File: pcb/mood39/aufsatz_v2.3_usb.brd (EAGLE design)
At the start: 21 x 29 mm, 9 parts

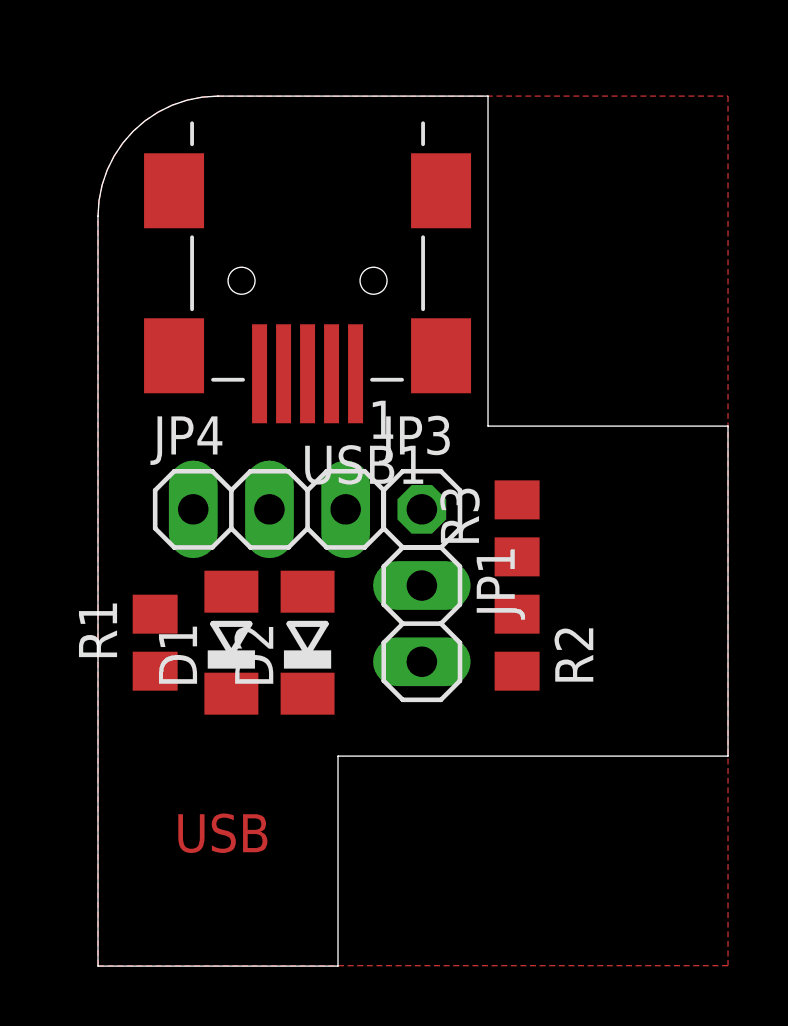
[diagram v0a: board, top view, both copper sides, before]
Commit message: replace mini usb connector
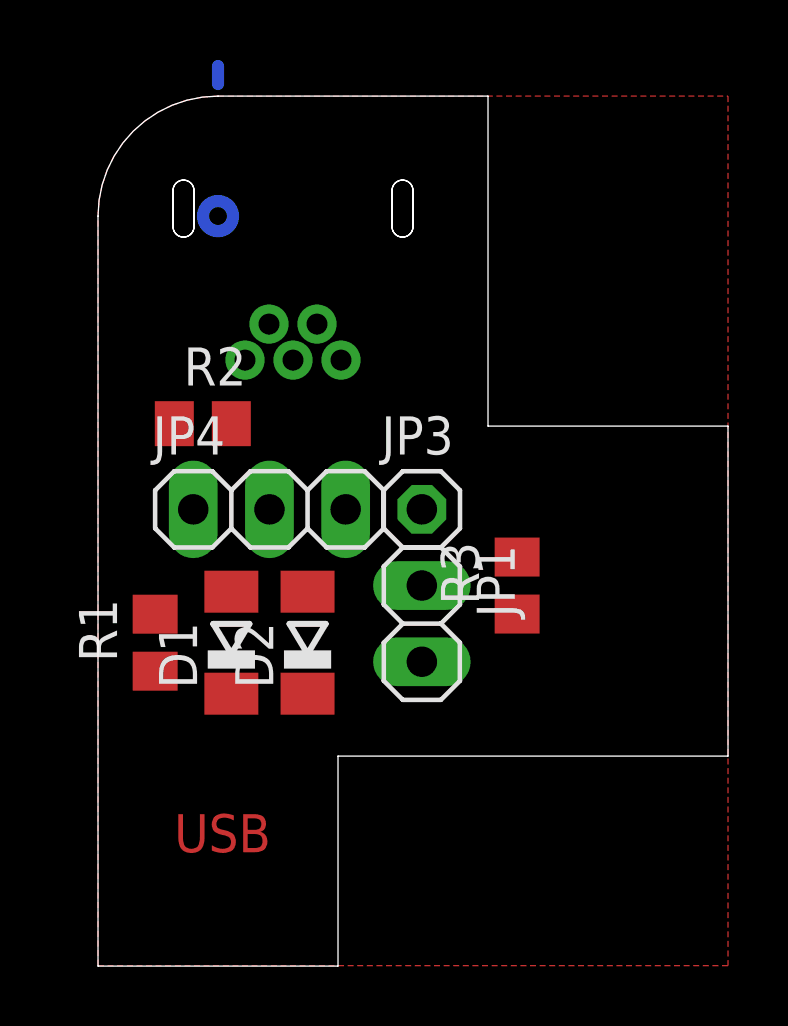
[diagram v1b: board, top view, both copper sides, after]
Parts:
- removed USB1: CON-USB-F-MINI-B, dp_devices:CONN_USB_MINI-B
- added U$1: USB_B_M-MINP, n39:USB_B_MINI-PRINT
- moved R2 12.8 mm to (3.49, 25.1), turned to 0 degrees
- moved R3 1.91 mm to (14.0, 19.7)
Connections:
- net GND: now also U$1.5; no longer USB1.GND
- net USBD+: now also U$1.3; no longer USB1.D+
- net USBD-: now also U$1.2; no longer USB1.D-
- net VCC: now also U$1.1; no longer USB1.VUSB
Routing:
- net N$1: track 0.00 -> 0.60 mm
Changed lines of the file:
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@@
 <setting verticaltext="up"/>
 </settings>
-<grid distance="25" unitdist="mil" unit="mil" style="dots" multiple="1" display="yes" altdistance="25" altunitdist="mil" altunit="mil"/>
+<grid distance="25" unitdist="mil" unit="mil" style="dots" multiple="1" display="yes" altdistance="12.5" altunitdist="mil" altunit="mil"/>
 <layers>
 <layer number="1" name="Top" color="4" fill="1" visible="yes" active="yes"/>
@@
 <layer number="23" name="tOrigins" color="15" fill="1" visible="yes" active="yes"/>
 <layer number="24" name="bOrigins" color="15" fill="1" visible="yes" active="yes"/>
-<layer number="25" name="tNames" color="7" fill="1" visible="no" active="yes"/>
-<layer number="26" name="bNames" color="7" fill="1" visible="no" active="yes"/>
-<layer number="27" name="tValues" color="7" fill="1" visible="no" active="yes"/>
-<layer number="28" name="bValues" color="7" fill="1" visible="no" active="yes"/>
+<layer number="25" name="tNames" color="7" fill="1" visible="yes" active="yes"/>
+<layer number="26" name="bNames" color="7" fill="1" visible="yes" active="yes"/>
+<layer number="27" name="tValues" color="7" fill="1" visible="yes" active="yes"/>
+<layer number="28" name="bValues" color="7" fill="1" visible="yes" active="yes"/>
 <layer number="29" name="tStop" color="7" fill="3" visible="no" active="yes"/>
 <layer number="30" name="bStop" color="7" fill="6" visible="no" active="yes"/>
@@
 <wire x1="8" y1="7" x2="8" y2="14" width="0" layer="20"/>
 <wire x1="8" y1="14" x2="21" y2="14" width="0" layer="20"/>
+<circle x="4" y="32" radius="0.5" width="0.4064" layer="16"/>
 </plain>
 <attributes>
@@
 <element name="JP1" library="pinhead" package="1X02" value="" x="10.795" y="18.415" rot="R270"/>
 <element name="R1" library="rcl" package="R0805" value="68R" x="1.905" y="17.78" rot="R90"/>
-<element name="R2" library="rcl" package="R0805" value="68R" x="13.97" y="17.78" rot="R270"/>
-<element name="R3" library="rcl" package="R0805" value="1k5" x="13.97" y="21.59" rot="R90"/>
+<element name="R2" library="rcl" package="R0805" value="68R" x="3.4925" y="25.0825"/>
+<element name="R3" library="rcl" package="R0805" value="1k5" x="13.97" y="19.685" rot="R90"/>
 <element name="D1" library="diode" package="SOD80C" value="3V6" x="4.445" y="17.78" rot="R90"/>
 <element name="D2" library="diode" package="SOD80C" value="3V6" x="6.985" y="17.78" rot="R90"/>
 <element name="JP3" library="pinhead" package="1X01" value="" x="10.795" y="22.225"/>
 <element name="JP4" library="pinhead" package="1X03" value="" x="5.715" y="22.225"/>
-<element name="USB1" library="dp_devices" package="CONN_USB_MINI-B" value="CON-USB-F-MINI-B" x="6.985" y="29.845" rot="R180"/>
+<element name="U$1" library="n39" package="USB_B_MINI-PRINT" value="USB_B_M-MINP" x="6.5" y="32.25" rot="MR270">
+<attribute name="REICHELT" value="USB BWM" x="6.5" y="32.25" size="1.778" layer="28" rot="MR270" display="off"/>
+</element>
 </elements>
 <signals>
@@
 <vertex x="21" y="7.015"/>
 </polygon>
-<contactref element="USB1" pad="GND"/>
-<wire x1="5.715" y1="22.225" x2="5.385" y2="26.745" width="0" layer="19" extent="1-1"/>
-<wire x1="6.985" y1="19.48" x2="5.715" y2="22.225" width="0" layer="19" extent="1-1"/>
-<wire x1="4.445" y1="19.48" x2="6.985" y2="19.48" width="0" layer="19" extent="1-1"/>
+<contactref element="U$1" pad="5"/>
 </signal>
 <signal name="SCK">
 <contactref element="R2" pad="2"/>
 <contactref element="JP4" pad="3"/>
-<wire x1="8.255" y1="22.225" x2="13.97" y2="16.83" width="0" layer="19" extent="1-1"/>
+<wire x1="4.4425" y1="25.0825" x2="8.255" y2="22.225" width="0" layer="19" extent="1-1"/>
 </signal>
 <signal name="VCC">
 <contactref element="R3" pad="2"/>
 <contactref element="JP3" pad="1"/>
-<contactref element="USB1" pad="VUSB"/>
-<wire x1="10.795" y1="22.225" x2="13.97" y2="22.54" width="0" layer="19" extent="1-1"/>
-<wire x1="8.585" y1="26.745" x2="10.795" y2="22.225" width="0" layer="19" extent="1-1"/>
+<contactref element="U$1" pad="1"/>
+<wire x1="10.795" y1="22.225" x2="13.97" y2="20.635" width="0" layer="19" extent="1-1"/>
+<wire x1="4.9" y1="27.2" x2="10.795" y2="22.225" width="0" layer="19" extent="1-1"/>
 </signal>
 <signal name="USBD-">
@@
 <contactref element="R3" pad="1"/>
 <contactref element="D1" pad="C"/>
-<contactref element="USB1" pad="D-"/>
-<wire x1="13.97" y1="18.73" x2="13.97" y2="20.64" width="0" layer="19" extent="1-1"/>
-<wire x1="10.795" y1="19.685" x2="13.97" y2="20.64" width="0" layer="19" extent="1-1"/>
-<wire x1="4.445" y1="16.08" x2="10.795" y2="19.685" width="0" layer="19" extent="1-1"/>
-<wire x1="7.785" y1="26.745" x2="10.795" y2="19.685" width="0" layer="19" extent="1-1"/>
+<contactref element="U$1" pad="2"/>
+<wire x1="2.5425" y1="25.0825" x2="5.7" y2="28.4" width="0" layer="19" extent="1-1"/>
+<wire x1="4.445" y1="16.08" x2="2.5425" y2="25.0825" width="0" layer="19" extent="1-1"/>
+<wire x1="10.795" y1="19.685" x2="4.445" y2="16.08" width="0" layer="19" extent="1-1"/>
+<wire x1="13.97" y1="18.735" x2="10.795" y2="19.685" width="0" layer="19" extent="1-1"/>
 </signal>
 <signal name="USBD+">
@@
 <contactref element="R1" pad="1"/>
 <contactref element="D2" pad="C"/>
-<contactref element="USB1" pad="D+"/>
-<wire x1="10.795" y1="17.145" x2="6.985" y2="26.745" width="0" layer="19" extent="1-1"/>
+<contactref element="U$1" pad="3"/>
+<wire x1="10.795" y1="17.145" x2="6.5" y2="27.2" width="0" layer="19" extent="1-1"/>
 <wire x1="6.985" y1="16.08" x2="10.795" y2="17.145" width="0" layer="19" extent="1-1"/>
 <wire x1="1.905" y1="16.83" x2="6.985" y2="16.08" width="0" layer="19" extent="1-1"/>
 </signal>
+<signal name="N$1">
+<wire x1="4" y1="36.4" x2="4" y2="37" width="0.4064" layer="16"/>
+</signal>
 </signals>
